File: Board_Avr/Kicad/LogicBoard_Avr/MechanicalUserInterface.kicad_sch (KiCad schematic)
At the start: 2 parts

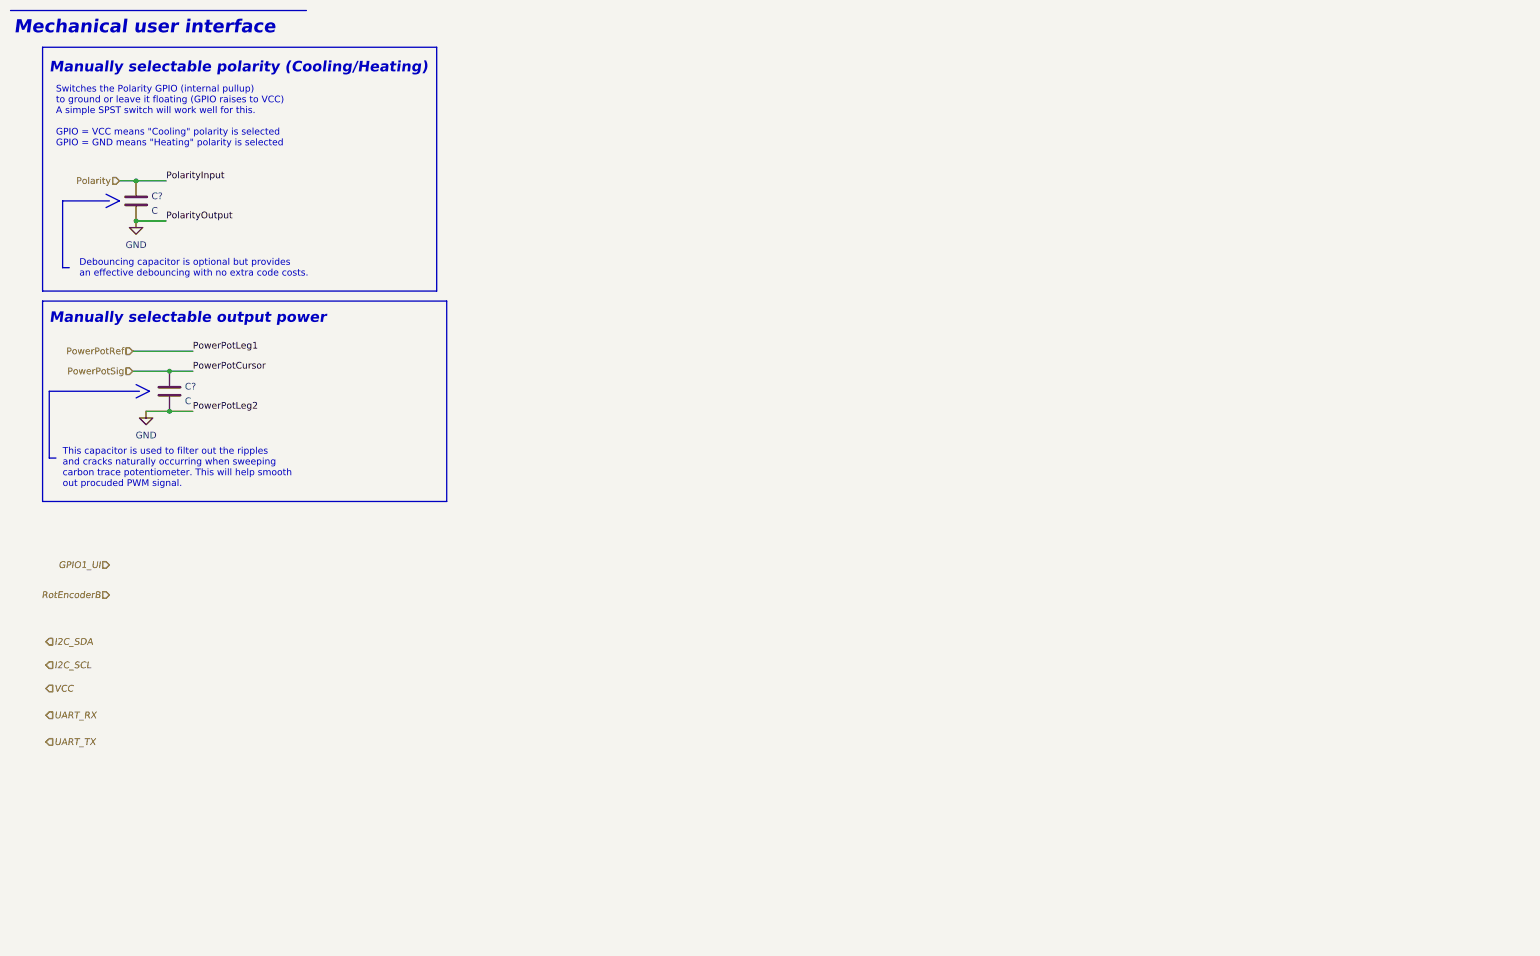
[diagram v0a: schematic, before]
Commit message: Designed basic layout for the mechanical user interface
Signed-off-by: bebenlebricolo <benoittarrade@hotmail.fr>
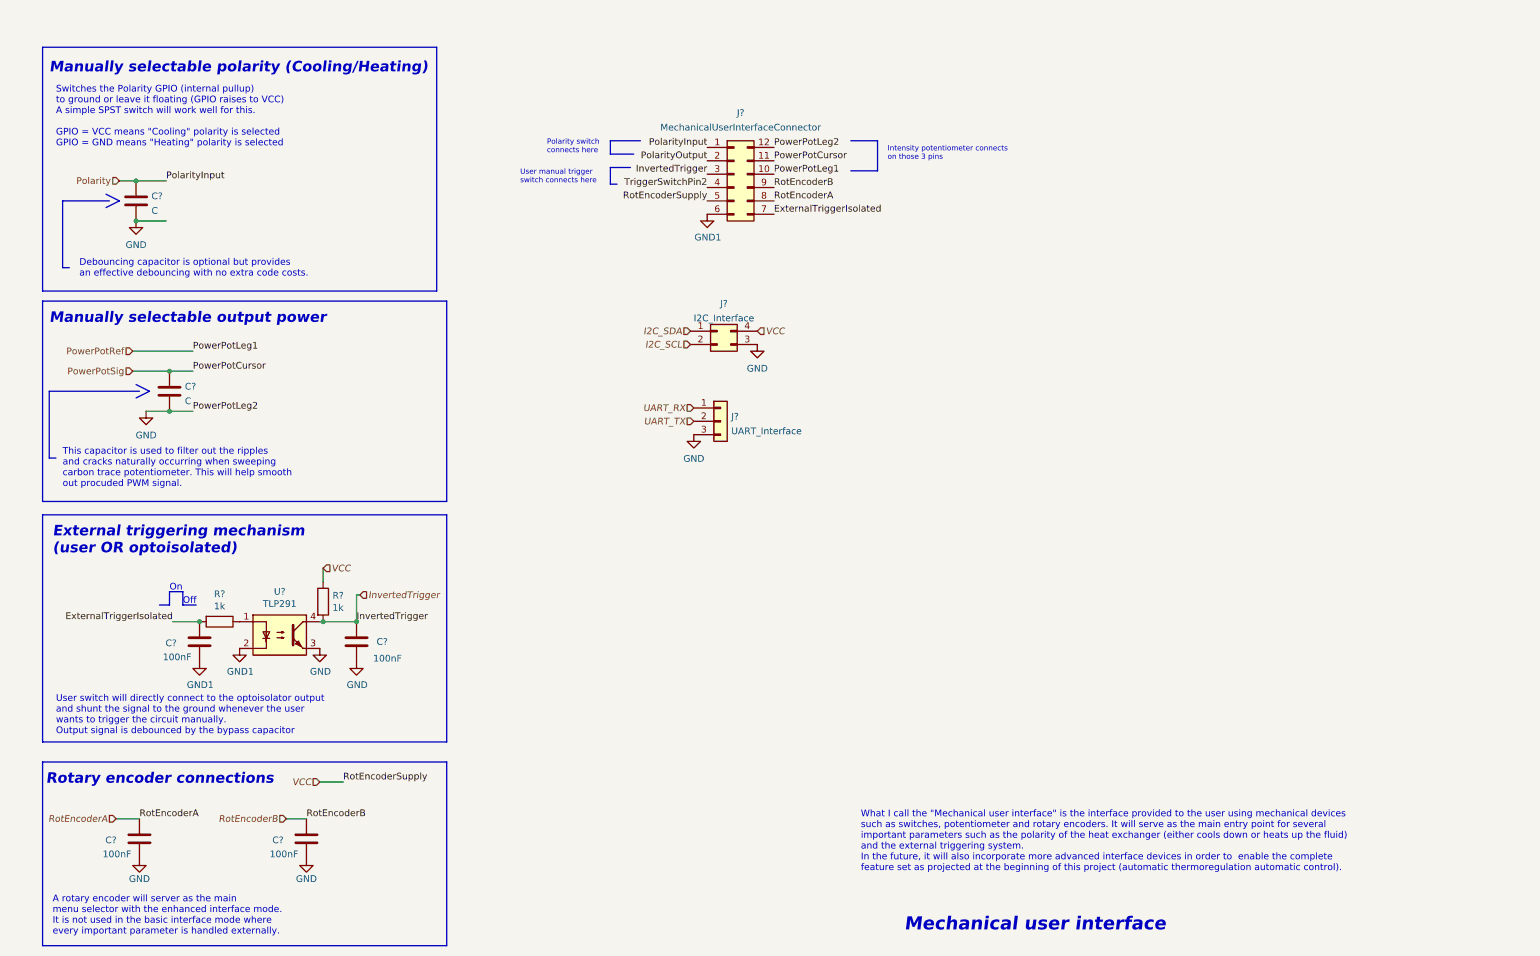
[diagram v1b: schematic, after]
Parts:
- added C? (x4): 100nF, Capacitor_SMD:C_1206_3216Metric_Pad1.33x1.80mm_HandSolder, symbol Device:C
- added J?: MechanicalUserInterfaceConnector, symbol Connector_Generic:Conn_02x06_Counter_Clockwise
- added J?: UART_Interface, symbol Connector_Generic:Conn_01x03
- added J?: I2C_Interface, symbol Connector_Generic:Conn_02x02_Counter_Clockwise
- added R? (x2): 1k, Resistor_SMD:R_1206_3216Metric_Pad1.30x1.75mm_HandSolder, symbol Device:R
- added U?: TLP291, Package_SO:SOIC-4_4.55x2.6mm_P1.27mm, symbol Isolator:TLP291
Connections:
- net GND: now also C?.1, C?.1, C?.1, J?.12 (Pin_12), J?.3 (Pin_3), J?.3 (Pin_3), U?.3
- net I2C_SCL: now also J?.2 (Pin_2)
- net I2C_SDA: now also J?.1 (Pin_1)
- net Polarity: now also J?.1 (Pin_1)
- net PowerPotRef: now also J?.10 (Pin_10)
- net PowerPotSig: now also J?.11 (Pin_11)
- net RotEncoderB: now also C?.2, J?.9 (Pin_9)
- net UART_RX: now also J?.1 (Pin_1)
- net UART_TX: now also J?.2 (Pin_2)
- net VCC: now also J?.4 (Pin_4), J?.5 (Pin_5), R?.1
- new net: R?.1, U?.1
- new net ExternalTriggerIsolated: C?.2, J?.7 (Pin_7), R?.2
- new net GND1: C?.1, J?.6 (Pin_6), U?.2
- new net InvertedTrigger: C?.2, J?.3 (Pin_3), R?.2, U?.4
- new net PolarityOutput: J?.2 (Pin_2)
- new net RotEncoderA: C?.2, J?.8 (Pin_8)
- new net TriggerSwitchPin2: J?.4 (Pin_4)
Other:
- note added: "A rotary encoder will server as the main menu selector with the enhanced interface mode. It is not used in the basic interface mode where every important parameter is handled externally."
- note added: "External triggering mechanism (user OR optoisolated)"
- note added: "Intensity potentiometer connects on those 3 pins"
- note added: "Off"
- note added: "On"
- note added: "Polarity switch connects here"
- note added: "Rotary encoder connections"
- note added: "User manual trigger switch connects here"
- note added: "User switch will directly connect to the optoisolator output and shunt the signal to the ground whenever the user wants to trigger the circuit manually. Output signal is debounced by the bypass capacitor"
- note added: "What I call the "Mechanical user interface" is the interface provided to the user using mechanical devices such as switches, potentiometer and rotary encoders. It will serve as the main entry point for several important parameters such as the polarity of the heat exchanger (either cools down or heats up the fluid) and the external triggering system. In the future, it will also incorporate more ad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"

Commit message: Added several other schematic sheets
Signed-off-by: bebenlebricolo <benoittarrade@hotmail.fr>
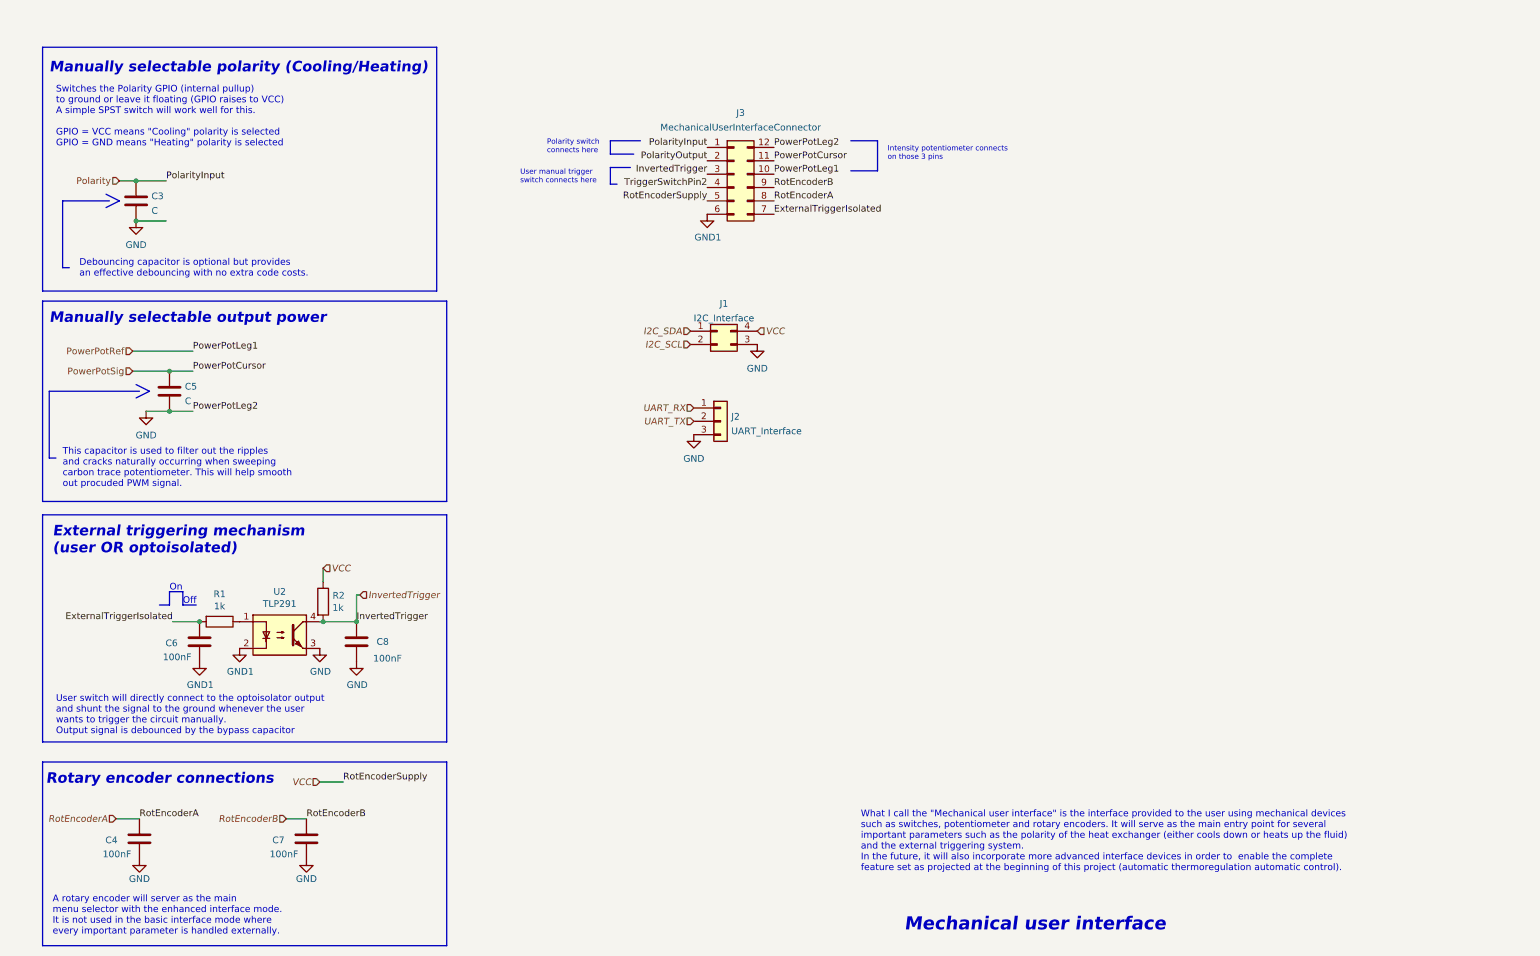
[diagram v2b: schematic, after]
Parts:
- gave numbers to parts that had none: 12
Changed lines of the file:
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@@
   (symbol (lib_id "power:GND") (at 75.565 137.795 0) (unit 1)
     (in_bom yes) (on_board yes)
-    (property "Reference" "#PWR?" (id 0) (at 75.565 144.145 0)
+    (property "Reference" "#PWR0108" (id 0) (at 75.565 144.145 0)
       (effects (font (size 1.27 1.27)) hide)
     )
@@
   (symbol (lib_id "Device:C") (at 46.99 88.9 0) (unit 1)
     (in_bom yes) (on_board yes) (fields_autoplaced)
-    (property "Reference" "C?" (id 0) (at 49.911 87.9915 0)
+    (property "Reference" "C5" (id 0) (at 49.911 87.9915 0)
       (effects (font (size 1.27 1.27)) (justify left))
     )
@@
   (symbol (lib_id "Connector_Generic:Conn_02x06_Counter_Clockwise") (at 154.305 47.625 0) (unit 1)
     (in_bom yes) (on_board yes)
-    (property "Reference" "J?" (id 0) (at 155.575 35.9599 0))
+    (property "Reference" "J3" (id 0) (at 155.575 35.9599 0))
     (property "Value" "MechanicalUserInterfaceConnector" (id 1) (at 155.575 38.735 0))
     (property "Footprint" "" (id 2) (at 154.305 47.625 0)
@@
   (symbol (lib_id "power:GND1") (at 149.225 55.245 0) (unit 1)
     (in_bom yes) (on_board yes)
-    (property "Reference" "#PWR?" (id 0) (at 149.225 61.595 0)
+    (property "Reference" "#PWR0107" (id 0) (at 149.225 61.595 0)
       (effects (font (size 1.27 1.27)) hide)
     )
@@
   (symbol (lib_id "power:GND") (at 73.025 177.8 0) (unit 1)
     (in_bom yes) (on_board yes)
-    (property "Reference" "#PWR?" (id 0) (at 73.025 184.15 0)
+    (property "Reference" "#PWR0114" (id 0) (at 73.025 184.15 0)
       (effects (font (size 1.27 1.27)) hide)
     )
@@
   (symbol (lib_id "power:GND") (at 82.55 140.335 0) (unit 1)
     (in_bom yes) (on_board yes)
-    (property "Reference" "#PWR?" (id 0) (at 82.55 146.685 0)
+    (property "Reference" "#PWR0110" (id 0) (at 82.55 146.685 0)
       (effects (font (size 1.27 1.27)) hide)
     )
@@
   (symbol (lib_id "power:GND") (at 41.275 177.8 0) (unit 1)
     (in_bom yes) (on_board yes)
-    (property "Reference" "#PWR?" (id 0) (at 41.275 184.15 0)
+    (property "Reference" "#PWR0115" (id 0) (at 41.275 184.15 0)
       (effects (font (size 1.27 1.27)) hide)
     )
@@
   (symbol (lib_id "Device:C") (at 52.705 136.525 180) (unit 1)
     (in_bom yes) (on_board yes)
-    (property "Reference" "C?" (id 0) (at 46.228 136.779 0)
+    (property "Reference" "C6" (id 0) (at 46.228 136.779 0)
       (effects (font (size 1.27 1.27)) (justify right))
     )
@@
   (symbol (lib_id "Isolator:TLP291") (at 67.945 135.255 0) (unit 1)
     (in_bom yes) (on_board yes)
-    (property "Reference" "U?" (id 0) (at 67.945 127 0))
+    (property "Reference" "U2" (id 0) (at 67.945 127 0))
     (property "Value" "TLP291" (id 1) (at 67.945 129.3114 0))
     (property "Footprint" "Package_SO:SOIC-4_4.55x2.6mm_P1.27mm" (id 2) (at 62.865 140.335 0)
@@
   (symbol (lib_id "power:GND1") (at 52.705 140.335 0) (unit 1)
     (in_bom yes) (on_board yes)
-    (property "Reference" "#PWR?" (id 0) (at 52.705 146.685 0)
+    (property "Reference" "#PWR0111" (id 0) (at 52.705 146.685 0)
       (effects (font (size 1.27 1.27)) hide)
     )
@@
   (symbol (lib_id "Device:C") (at 41.275 173.99 180) (unit 1)
     (in_bom yes) (on_board yes)
-    (property "Reference" "C?" (id 0) (at 34.798 174.244 0)
+    (property "Reference" "C4" (id 0) (at 34.798 174.244 0)
       (effects (font (size 1.27 1.27)) (justify right))
     )
@@
   (symbol (lib_id "Device:R") (at 76.2 128.905 0) (unit 1)
     (in_bom yes) (on_board yes)
-    (property "Reference" "R?" (id 0) (at 77.978 127.7366 0)
+    (property "Reference" "R2" (id 0) (at 77.978 127.7366 0)
       (effects (font (size 1.27 1.27)) (justify left))
     )
@@
   (symbol (lib_id "power:GND") (at 146.685 97.155 0) (unit 1)
     (in_bom yes) (on_board yes) (fields_autoplaced)
-    (property "Reference" "#PWR?" (id 0) (at 146.685 103.505 0)
+    (property "Reference" "#PWR0106" (id 0) (at 146.685 103.505 0)
       (effects (font (size 1.27 1.27)) hide)
     )
@@
   (symbol (lib_id "power:GND1") (at 60.325 137.795 0) (unit 1)
     (in_bom yes) (on_board yes)
-    (property "Reference" "#PWR?" (id 0) (at 60.325 144.145 0)
+    (property "Reference" "#PWR0109" (id 0) (at 60.325 144.145 0)
       (effects (font (size 1.27 1.27)) hide)
     )
@@
   (symbol (lib_id "Device:C") (at 73.025 173.99 180) (unit 1)
     (in_bom yes) (on_board yes)
-    (property "Reference" "C?" (id 0) (at 66.548 174.244 0)
+    (property "Reference" "C7" (id 0) (at 66.548 174.244 0)
       (effects (font (size 1.27 1.27)) (justify right))
     )
@@
   (symbol (lib_id "Device:C") (at 82.55 136.525 180) (unit 1)
     (in_bom yes) (on_board yes)
-    (property "Reference" "C?" (id 0) (at 86.36 136.525 0)
+    (property "Reference" "C8" (id 0) (at 86.36 136.525 0)
       (effects (font (size 1.27 1.27)) (justify right))
     )
@@
   (symbol (lib_id "Connector_Generic:Conn_01x03") (at 151.765 94.615 0) (unit 1)
     (in_bom yes) (on_board yes)
-    (property "Reference" "J?" (id 0) (at 153.797 93.7065 0)
+    (property "Reference" "J2" (id 0) (at 153.797 93.7065 0)
       (effects (font (size 1.27 1.27)) (justify left))
     )
@@
   (symbol (lib_id "Connector_Generic:Conn_02x02_Counter_Clockwise") (at 151.13 77.47 0) (unit 1)
     (in_bom yes) (on_board yes) (fields_autoplaced)
-    (property "Reference" "J?" (id 0) (at 152.4 72.2335 0))
+    (property "Reference" "J1" (id 0) (at 152.4 72.2335 0))
     (property "Value" "I2C_Interface" (id 1) (at 152.4 75.0086 0))
     (property "Footprint" "" (id 2) (at 151.13 77.47 0)
@@
   (symbol (lib_id "Device:C") (at 40.64 52.705 0) (unit 1)
     (in_bom yes) (on_board yes) (fields_autoplaced)
-    (property "Reference" "C?" (id 0) (at 43.561 51.7965 0)
+    (property "Reference" "C3" (id 0) (at 43.561 51.7965 0)
       (effects (font (size 1.27 1.27)) (justify left))
     )
@@
   (symbol (lib_id "power:GND") (at 158.75 80.01 0) (unit 1)
     (in_bom yes) (on_board yes) (fields_autoplaced)
-    (property "Reference" "#PWR?" (id 0) (at 158.75 86.36 0)
+    (property "Reference" "#PWR0105" (id 0) (at 158.75 86.36 0)
       (effects (font (size 1.27 1.27)) hide)
     )
@@
   (symbol (lib_id "Device:R") (at 56.515 132.715 270) (unit 1)
     (in_bom yes) (on_board yes)
-    (property "Reference" "R?" (id 0) (at 56.515 127.4572 90))
+    (property "Reference" "R1" (id 0) (at 56.515 127.4572 90))
     (property "Value" "1k" (id 1) (at 56.515 129.7686 90))
     (property "Footprint" "Resistor_SMD:R_1206_3216Metric_Pad1.30x1.75mm_HandSolder" (id 2) (at 56.515 130.937 90)
